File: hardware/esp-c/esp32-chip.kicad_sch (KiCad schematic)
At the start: 26 parts, among them U12 ESP32-WROOM-32E(4MB), U3 SS8050_C2150, U8 SS8050_C2150

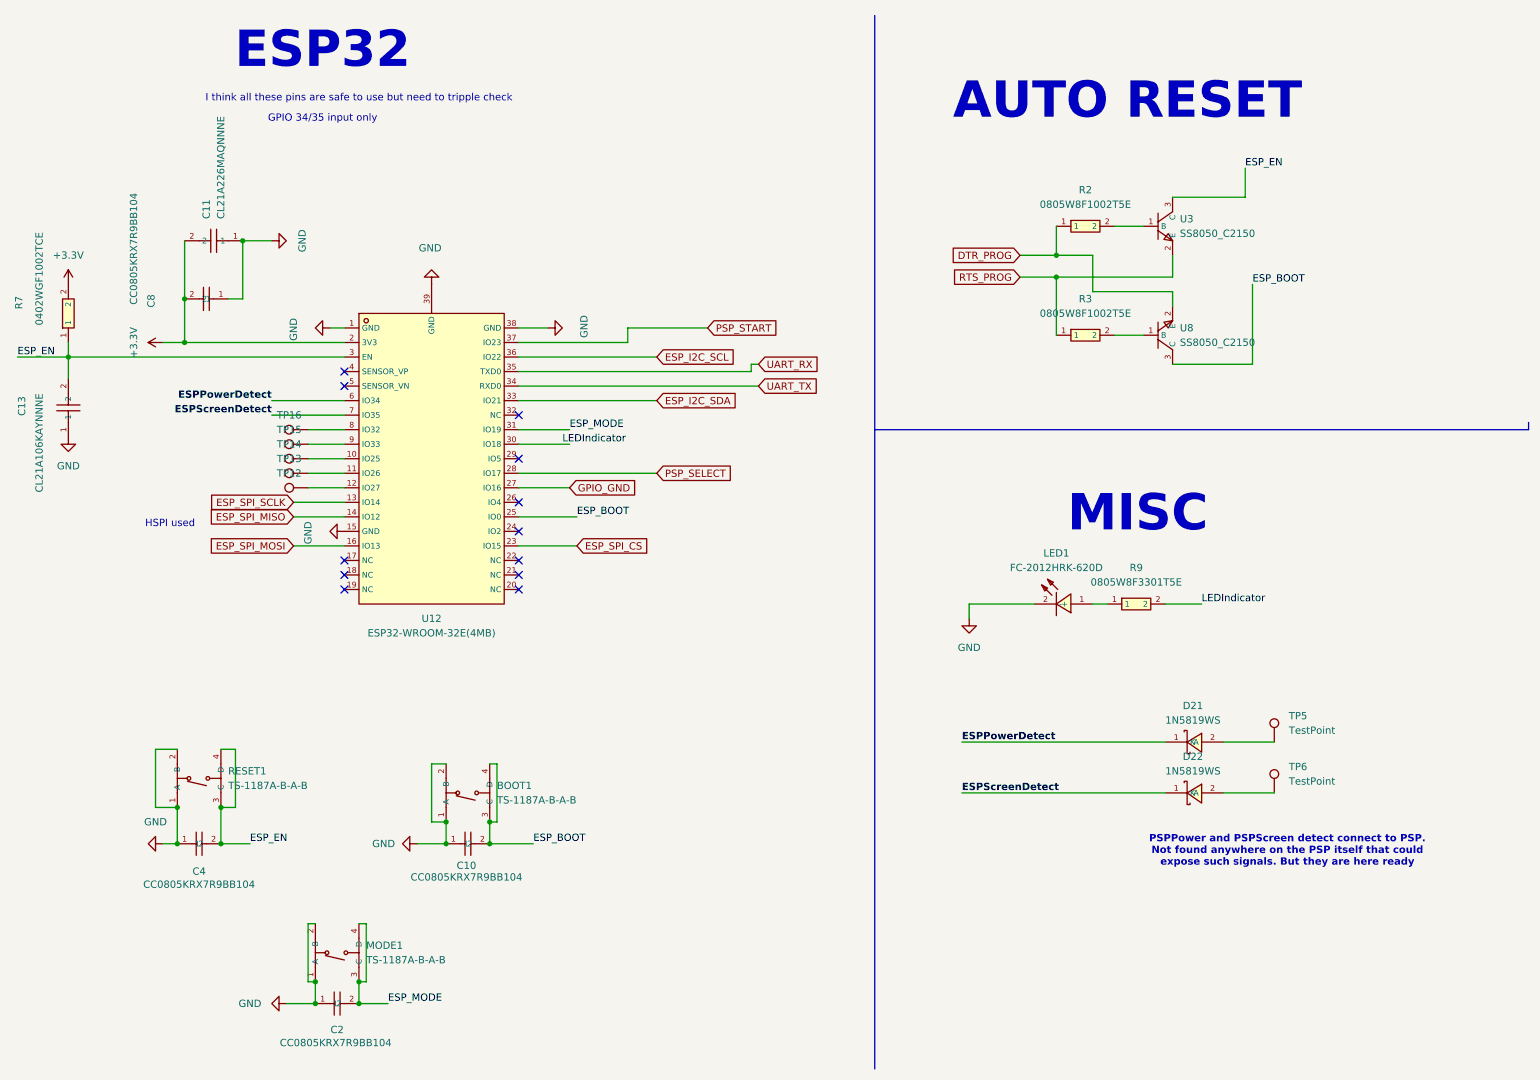
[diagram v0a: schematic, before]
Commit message: [Hardware] Added LED pad and changed switch to right angle
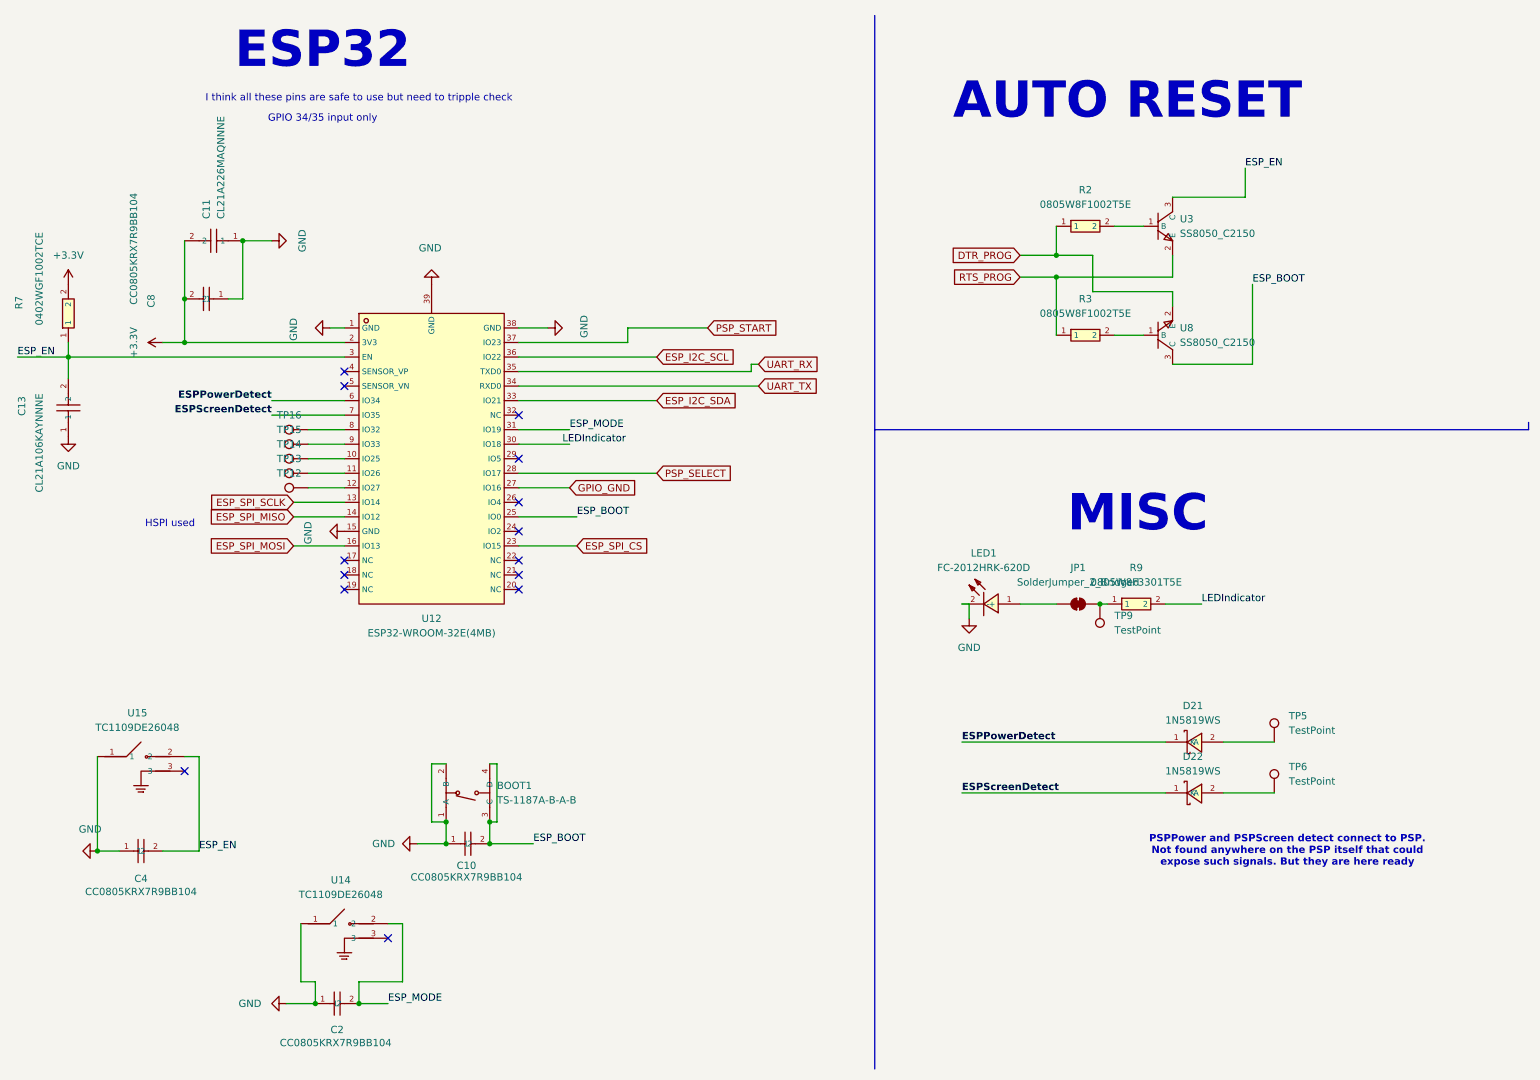
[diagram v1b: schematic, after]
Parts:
- removed MODE1, RESET1: TS-1187A-B-A-B, JLCPCB_footprint:SW-SMD_4P-L5.1-W5.1-P3.70-LS6.5-TL-2, symbol JLCPCB_schematic:TS-1187A-B-A-B
- added JP1: SolderJumper_2_Bridged, Jumper:SolderJumper-2_P1.3mm_Bridged_Pad1.0x1.5mm, symbol Jumper:SolderJumper_2_Bridged
- added TP9: TestPoint, TestPoint:TestPoint_Pad_1.0x1.0mm, symbol Connector:TestPoint
- added U14, U15: TC1109DE26048, JLCPCB_footprint:SW-TH_3P-L4.5-W4.5-P1.8-LS3.0, symbol JLCPCB_schematic:TC1109DE26048
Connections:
- net ESP_EN: now also U15.2
- net ESP_MODE: now also U14.2
- net GND: now also U14.1, U15.1
- net at R9.1: now also JP1.2 (B), TP9.1; no longer LED1.1 (+)
- new net: JP1.1 (A), LED1.1 (+)
- no-connect marks 12 -> 14
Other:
- moved on the sheet: C4, LED1
